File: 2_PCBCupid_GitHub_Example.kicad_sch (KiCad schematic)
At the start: 6 parts, among them J1 Conn_01x02, SW1 SW_MEC_5G

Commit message: THT component added
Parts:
- R1: footprint (none) -> Resistor_THT:R_Axial_DIN0207_L6.3mm_D2.5mm_P2.54mm_Vertical
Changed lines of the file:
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@@
 			)
 		)
-		(property "Footprint" ""
+		(property "Footprint" "Resistor_THT:R_Axial_DIN0207_L6.3mm_D2.5mm_P2.54mm_Vertical"
 			(at 129.032 111.76 90)
 			(effects

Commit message: all components added to the board missing layout and routing
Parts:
- D1, D2: footprint (none) -> LED_THT:LED_D5.0mm
- J1: footprint (none) -> Connector_PinHeader_2.54mm:PinHeader_1x02_P2.54mm_Vertical
- R2: footprint (none) -> Resistor_THT:R_Axial_DIN0207_L6.3mm_D2.5mm_P2.54mm_Vertical
- SW1: footprint (none) -> Button_Switch_THT:SW_PUSH_6mm
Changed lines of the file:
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@@
 			)
 		)
-		(property "Footprint" ""
+		(property "Footprint" "LED_THT:LED_D5.0mm"
 			(at 130.81 102.87 0)
 			(effects
@@
 			)
 		)
-		(property "Footprint" ""
+		(property "Footprint" "LED_THT:LED_D5.0mm"
 			(at 118.11 102.87 0)
 			(effects
@@
 			)
 		)
-		(property "Footprint" ""
+		(property "Footprint" "Resistor_THT:R_Axial_DIN0207_L6.3mm_D2.5mm_P2.54mm_Vertical"
 			(at 116.332 111.76 90)
 			(effects
@@
 			)
 		)
-		(property "Footprint" ""
+		(property "Footprint" "Connector_PinHeader_2.54mm:PinHeader_1x02_P2.54mm_Vertical"
 			(at 154.94 105.41 0)
 			(effects
@@
 			)
 		)
-		(property "Footprint" ""
+		(property "Footprint" "Button_Switch_THT:SW_PUSH_6mm"
 			(at 125.73 91.44 0)
 			(effects

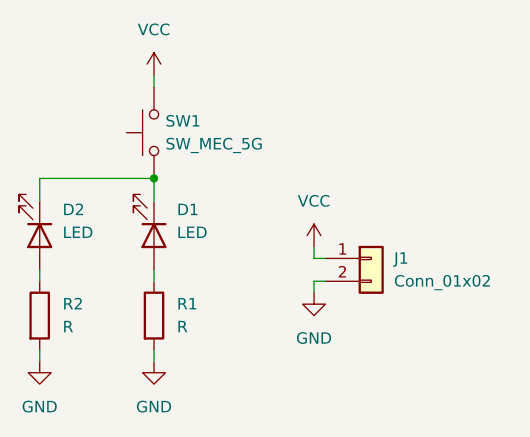
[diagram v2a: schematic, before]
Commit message: Fixed swithc 2 schematic and pcb layout
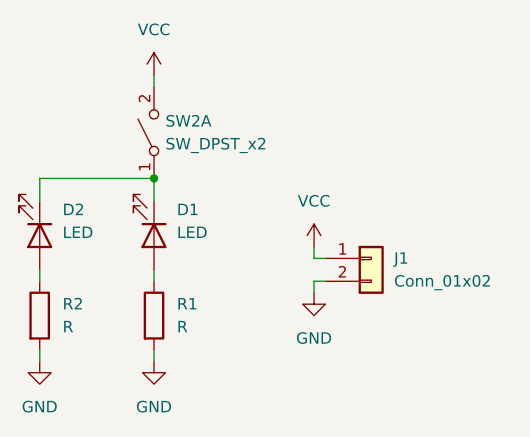
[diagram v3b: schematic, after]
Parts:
- removed SW1: SW_MEC_5G, Button_Switch_THT:SW_PUSH_6mm, symbol Switch:SW_MEC_5G
- added SW2: SW_DPST_x2, Button_Switch_THT:SW_PUSH_6mm, symbol Switch:SW_DPST_x2
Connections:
- net VCC: now also SW2.2 (B)
- net at D1.1 (K), D2.1 (K): now also SW2.1 (A)
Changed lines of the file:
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@@
+	)
+	(symbol
+		(lib_id "Switch:SW_DPST_x2")
+		(at 130.81 91.44 90)
+		(unit 1)
+		(exclude_from_sim no)
+		(in_bom yes)
+		(on_board yes)
+		(dnp no)
+		(fields_autoplaced yes)
+		(property "Reference" "SW2"
+			(at 132.08 90.1699 90)
+			(effects
+				(font
+					(size 1.27 1.27)
+				)
+				(justify right)
+			)
+		)
+		(property "Value" "SW_DPST_x2"
+			(at 132.08 92.7099 90)
+			(effects
+				(font
+					(size 1.27 1.27)
+				)
+				(justify right)
+			)
+		)
+		(property "Footprint" "Button_Switch_THT:SW_PUSH_6mm"
+			(at 130.81 91.44 0)
+			(effects
+				(font
+					(size 1.27 1.27)
+				)
+				(hide yes)
+			)
+		)
+		(property "Datasheet" "~"
+			(at 130.81 91.44 0)
+			(effects
+				(font
+					(size 1.27 1.27)
+				)
+				(hide yes)
+			)
+		)
+		(property "Description" "Single Pole Single Throw (SPST) switch, separate symbol"
+			(at 130.81 91.44 0)
+			(effects
+				(font
+					(size 1.27 1.27)
+				)
+				(hide yes)
+			)
+		)
+		(pin "4"
+		)
+		(pin "1"
+		)
+		(pin "2"
+		)
+		(pin "3"
+		)
+		(instances
+			(project ""
+				(path "/c2af59b7-a490-43ea-8acf-dde769c9e4ce"
+					(reference "SW2")
+					(unit 1)
+				)
+			)
+		)
 	)
 	(symbol
@@
 					(unit 1)
 				)
-			)
-		)
-	)
-	(symbol
-		(lib_id "Switch:SW_MEC_5G")
-		(at 130.81 91.44 90)
-		(unit 1)
-		(exclude_from_sim no)
-		(in_bom yes)
-		(on_board yes)
-		(dnp no)
-		(fields_autoplaced yes)
-		(property "Reference" "SW1"
-			(at 132.08 90.1699 90)
-			(effects
-				(font
-					(size 1.27 1.27)
-				)
-				(justify right)
-			)
-		)
-		(property "Value" "SW_MEC_5G"
-			(at 132.08 92.7099 90)
-			(effects
-				(font
-					(size 1.27 1.27)
-				)
-				(justify right)
-			)
-		)
-		(property "Footprint" "Button_Switch_THT:SW_PUSH_6mm"
-			(at 125.73 91.44 0)
-			(effects
-				(font
-					(size 1.27 1.27)
-				)
-				(hide yes)
-			)
-		)
-		(property "Datasheet" "http://www.apem.com/int/index.php?controller=attachment&id_attachment=488"
-			(at 125.73 91.44 0)
-			(effects
-				(font
-					(size 1.27 1.27)
-				)
-				(hide yes)
-			)
-		)
-		(property "Description" "MEC 5G single pole normally-open tactile switch"
-			(at 130.81 91.44 0)
-			(effects
-				(font
-					(size 1.27 1.27)
-				)
-				(hide yes)
-			)
-		)
-		(pin "1"
-		)
-		(pin "4"
-		)
-		(pin "3"
-		)
-		(pin "2"
-		)
-		(instances
-			(project ""
-				(path "/c2af59b7-a490-43ea-8acf-dde769c9e4ce"
-					(reference "SW1")
-					(unit 1)
-				)

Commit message: SMD schematic and layout completed
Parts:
- D1, D2: footprint LED_THT:LED_D5.0mm -> LED_SMD:LED_0805_2012Metric
- J1: footprint Connector_PinHeader_2.54mm:PinHeader_1x02_P2.54mm_Vertical -> Connector_PinHeader_2.54mm:PinHeader_1x02_P2.54mm_Vertical_SMD_Pin1Left
- R1, R2: footprint Resistor_THT:R_Axial_DIN0207_L6.3mm_D2.5mm_P2.54mm_Vertical -> Resistor_SMD:R_0805_2012Metric
- SW2: footprint Button_Switch_THT:SW_PUSH_6mm -> Button_Switch_SMD:SW_Push_1P1T_NO_CK_KMR2
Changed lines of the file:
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@@
 			)
 		)
-		(property "Footprint" "LED_THT:LED_D5.0mm"
+		(property "Footprint" "LED_SMD:LED_0805_2012Metric"
 			(at 130.81 102.87 0)
 			(effects
@@
 			)
 		)
-		(property "Footprint" "LED_THT:LED_D5.0mm"
+		(property "Footprint" "LED_SMD:LED_0805_2012Metric"
 			(at 118.11 102.87 0)
 			(effects
@@
 			)
 		)
-		(property "Footprint" "Resistor_THT:R_Axial_DIN0207_L6.3mm_D2.5mm_P2.54mm_Vertical"
+		(property "Footprint" "Resistor_SMD:R_0805_2012Metric"
 			(at 116.332 111.76 90)
 			(effects
@@
 			)
 		)
-		(property "Footprint" "Button_Switch_THT:SW_PUSH_6mm"
+		(property "Footprint" "Button_Switch_SMD:SW_Push_1P1T_NO_CK_KMR2"
 			(at 130.81 91.44 0)
 			(effects
@@
 			)
 		)
-		(property "Footprint" "Resistor_THT:R_Axial_DIN0207_L6.3mm_D2.5mm_P2.54mm_Vertical"
+		(property "Footprint" "Resistor_SMD:R_0805_2012Metric"
 			(at 129.032 111.76 90)
 			(effects
@@
 			)
 		)
-		(property "Footprint" "Connector_PinHeader_2.54mm:PinHeader_1x02_P2.54mm_Vertical"
+		(property "Footprint" "Connector_PinHeader_2.54mm:PinHeader_1x02_P2.54mm_Vertical_SMD_Pin1Left"
 			(at 154.94 105.41 0)
 			(effects
